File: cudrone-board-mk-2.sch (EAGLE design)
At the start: 61 parts, among them Q1 BSS138, U1 EDISON_CONNECTOR_FULLMOUNTING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, U2 FTS31XS-U, U4 TPS62065, U5 USD-SOCKETNEW, U6 TXB0108, U8 PCA9306, U9 MIC5205

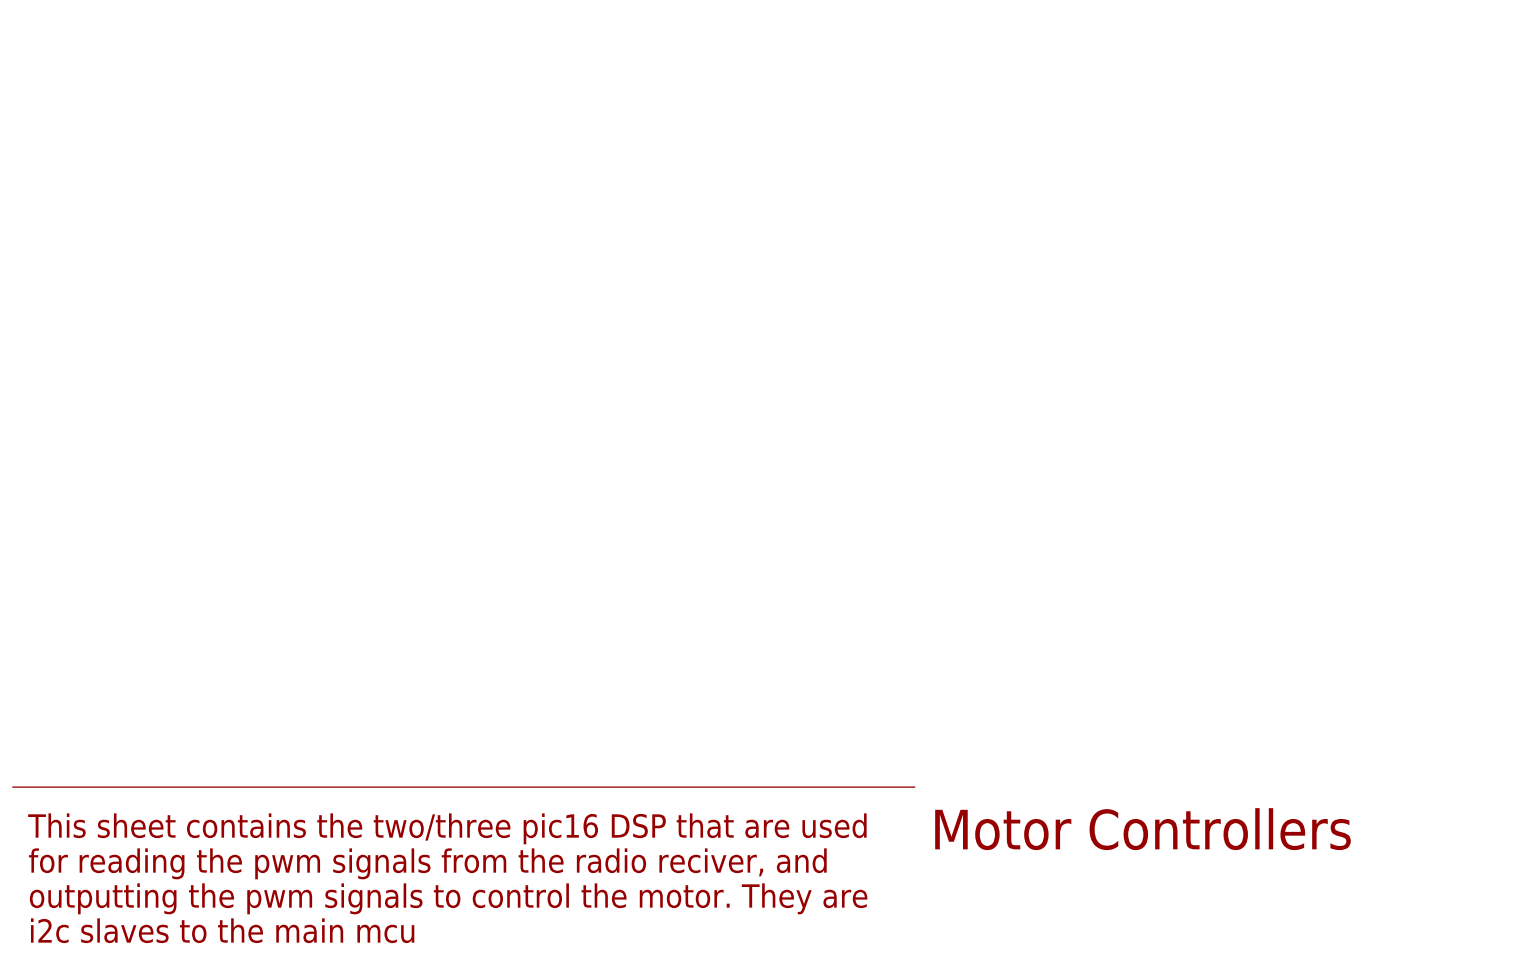
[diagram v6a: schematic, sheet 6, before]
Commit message: Added new port for servos on the motors to be connected. Picked a dsp to be used to control the motors
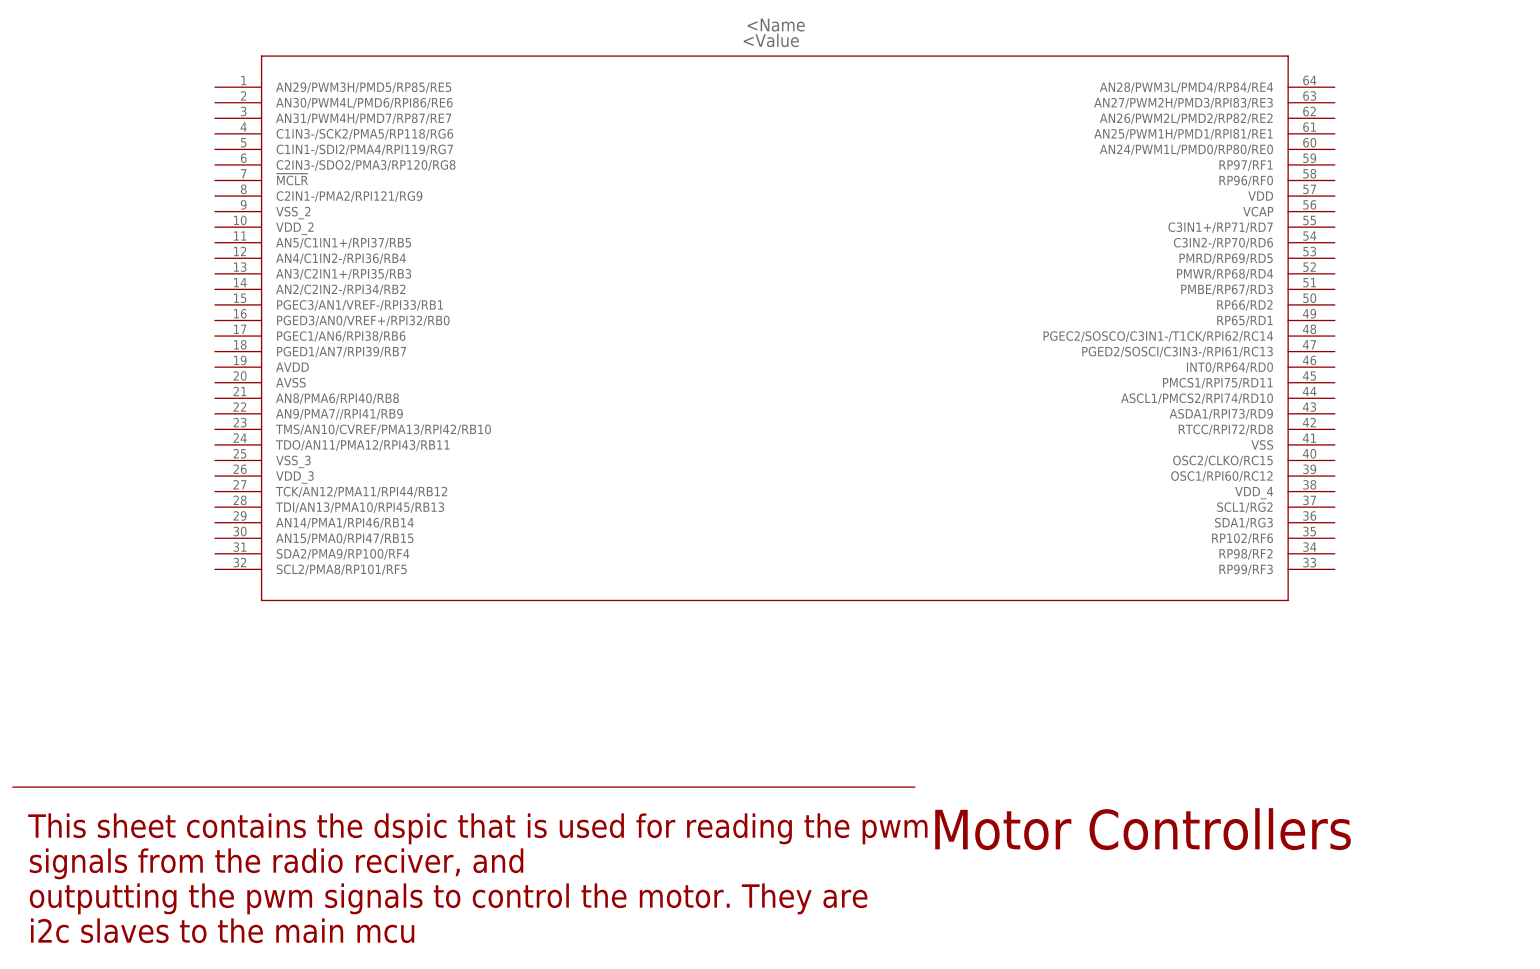
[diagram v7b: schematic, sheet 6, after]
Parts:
- added MOTOR_SERVO: 3X8, Drone_Connectors:3X8
- added U$4: DSPIC33EP512MC806-I/PT, DSPIC33EP512MC806:DSPIC33EP512MC806-I/PT
- renumbered SERVOS to GIMBAL_SERVOS
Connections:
- new net MS1: MOTOR_SERVO.8
- new net MS2: MOTOR_SERVO.7
- new net MS3: MOTOR_SERVO.6
- new net MS4: MOTOR_SERVO.5
- new net MS5: MOTOR_SERVO.4
- new net MS6: MOTOR_SERVO.3
- new net MS7: MOTOR_SERVO.2
- new net MS8: MOTOR_SERVO.1
- net 5V: now also MOTOR_SERVO.V
- net GND: now also MOTOR_SERVO.G
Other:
- note added: "This sheet contains the dspic that is used for reading the pwm signals from the radio reciver, and outputting the pwm signals to control the motor. They are i2c slaves to the main mcu"
- note removed: "This sheet contains the two/three pic16 DSP that are used for reading the pwm signals from the radio reciver, and outputting the pwm signals to control the motor. They are i2c slaves to the main mcu"
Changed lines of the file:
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@@
 <?xml version="1.0" encoding="utf-8"?>
 <!DOCTYPE eagle SYSTEM "eagle.dtd">
-<eagle version="6.5.0">
+<eagle version="8.0.0">
 <drawing>
 <settings>
@@
 <part name="SUPPLY22" library="SparkFun-Aesthetics" deviceset="1.8V" device=""/>
 <part name="SUPPLY23" library="SparkFun-Aesthetics" deviceset="1.8V" device=""/>
-<part name="SERVOS" library="Drone_Connectors" deviceset="3X4" device=""/>
+<part name="GIMBAL_SERVOS" library="Drone_Connectors" deviceset="3X4" device=""/>
 <part name="RECIVER" library="Drone_Connectors" deviceset="3X8" device=""/>
 <part name="ESC" library="Drone_Connectors" deviceset="3X8" device=""/>
@@
 <part name="GND35" library="SparkFun-Aesthetics" deviceset="GND" device=""/>
 <part name="GND36" library="SparkFun-Aesthetics" deviceset="GND" device=""/>
+<part name="MOTOR_SERVO" library="Drone_Connectors" deviceset="3X8" device=""/>
+<part name="SUPPLY27" library="SparkFun-Aesthetics" deviceset="5V" device=""/>
+<part name="GND37" library="SparkFun-Aesthetics" deviceset="GND" device=""/>
+<part name="U$4" library="DSPIC33EP512MC806" deviceset="DSPIC33EP512MC806-I/PT" device=""/>
 </parts>
 <sheets>
@@
 <text x="149.86" y="25.4" size="6.4516" layer="94">Motor Controllers</text>
 <wire x1="147.32" y1="35.56" x2="0" y2="35.56" width="0.1524" layer="94"/>
-<text x="2.54" y="10.16" size="3.81" layer="94">This sheet contains the two/three pic16 DSP that are used
-for reading the pwm signals from the radio reciver, and
+<text x="2.54" y="10.16" size="3.81" layer="94">This sheet contains the dspic that is used for reading the pwm
+signals from the radio reciver, and
 outputting the pwm signals to control the motor. They are
 i2c slaves to the main mcu</text>
@@
 <instance part="FRAME6" gate="G$1" x="0" y="0"/>
 <instance part="FRAME6" gate="G$2" x="147.32" y="0"/>
+<instance part="U$4" gate="A" x="33.02" y="149.86"/>
 </instances>
 <busses>
@@
 <instance part="FRAME9" gate="G$1" x="0" y="0"/>
 <instance part="FRAME9" gate="G$2" x="147.32" y="0"/>
-<instance part="SERVOS" gate="G$1" x="114.3" y="160.02"/>
+<instance part="GIMBAL_SERVOS" gate="G$1" x="114.3" y="160.02"/>
 <instance part="RECIVER" gate="G$1" x="114.3" y="129.54"/>
 <instance part="ESC" gate="G$1" x="114.3" y="91.44"/>
@@
 <instance part="GND35" gate="1" x="106.68" y="114.3"/>
 <instance part="GND36" gate="1" x="106.68" y="149.86"/>
+<instance part="MOTOR_SERVO" gate="G$1" x="114.3" y="55.88"/>
+<instance part="SUPPLY27" gate="G$1" x="106.68" y="66.04"/>
+<instance part="GND37" gate="1" x="106.68" y="40.64"/>
 </instances>
 <busses>
@@
 <pinref part="GND36" gate="1" pin="GND"/>
 <wire x1="106.68" y1="152.4" x2="106.68" y2="154.94" width="0.1524" layer="91"/>
-<pinref part="SERVOS" gate="G$1" pin="G"/>
+<pinref part="GIMBAL_SERVOS" gate="G$1" pin="G"/>
 <wire x1="106.68" y1="154.94" x2="109.22" y2="154.94" width="0.1524" layer="91"/>
 </segment>
@@
 <wire x1="106.68" y1="81.28" x2="109.22" y2="81.28" width="0.1524" layer="91"/>
 </segment>
+<segment>
+<pinref part="MOTOR_SERVO" gate="G$1" pin="G"/>
+<pinref part="GND37" gate="1" pin="GND"/>
+<wire x1="109.22" y1="45.72" x2="106.68" y2="45.72" width="0.1524" layer="91"/>
+<wire x1="106.68" y1="45.72" x2="106.68" y2="43.18" width="0.1524" layer="91"/>
+</segment>
 </net>
 <net name="5V" class="0">
@@
 <pinref part="SUPPLY24" gate="G$1" pin="5V"/>
 <wire x1="106.68" y1="165.1" x2="106.68" y2="162.56" width="0.1524" layer="91"/>
-<pinref part="SERVOS" gate="G$1" pin="V"/>
+<pinref part="GIMBAL_SERVOS" gate="G$1" pin="V"/>
 <wire x1="106.68" y1="162.56" x2="109.22" y2="162.56" width="0.1524" layer="91"/>
 </segment>
@@
 <wire x1="106.68" y1="99.06" x2="109.22" y2="99.06" width="0.1524" layer="91"/>
 </segment>
+<segment>
+<pinref part="MOTOR_SERVO" gate="G$1" pin="V"/>
+<pinref part="SUPPLY27" gate="G$1" pin="5V"/>
+<wire x1="109.22" y1="63.5" x2="106.68" y2="63.5" width="0.1524" layer="91"/>
+<wire x1="106.68" y1="63.5" x2="106.68" y2="66.04" width="0.1524" layer="91"/>
+</segment>
 </net>
 <net name="GP12_PWM0" class="0">
 <segment>
-<pinref part="SERVOS" gate="G$1" pin="S4"/>
+<pinref part="GIMBAL_SERVOS" gate="G$1" pin="S4"/>
 <wire x1="121.92" y1="162.56" x2="124.46" y2="162.56" width="0.1524" layer="91"/>
 <label x="124.46" y="162.56" size="1.778" layer="95" xref="yes"/>
@@
 <net name="GP13_PWM1" class="0">
 <segment>
-<pinref part="SERVOS" gate="G$1" pin="S3"/>
+<pinref part="GIMBAL_SERVOS" gate="G$1" pin="S3"/>
 <wire x1="121.92" y1="160.02" x2="147.32" y2="160.02" width="0.1524" layer="91"/>
 <label x="147.32" y="160.02" size="1.778" layer="95" xref="yes"/>
@@
 <net name="GP182_PWM2" class="0">
 <segment>
-<pinref part="SERVOS" gate="G$1" pin="S2"/>
+<pinref part="GIMBAL_SERVOS" gate="G$1" pin="S2"/>
 <wire x1="121.92" y1="157.48" x2="124.46" y2="157.48" width="0.1524" layer="91"/>
 <label x="124.46" y="157.48" size="1.778" layer="95" xref="yes"/>
@@
 <net name="GP183_PWM3" class="0">
 <segment>
-<pinref part="SERVOS" gate="G$1" pin="S1"/>
+<pinref part="GIMBAL_SERVOS" gate="G$1" pin="S1"/>
 <wire x1="121.92" y1="154.94" x2="147.32" y2="154.94" width="0.1524" layer="91"/>
 <label x="147.32" y="154.94" size="1.778" layer="95" xref="yes"/>
@@
 </segment>
 </net>
+<net name="MS1" class="0">
+<segment>
+<pinref part="MOTOR_SERVO" gate="G$1" pin="8"/>
+<wire x1="121.92" y1="63.5" x2="124.46" y2="63.5" width="0.1524" layer="91"/>
+<label x="121.92" y="63.5" size="1.778" layer="95"/>
+</segment>
+</net>
+<net name="MS2" class="0">
+<segment>
+<pinref part="MOTOR_SERVO" gate="G$1" pin="7"/>
+<wire x1="121.92" y1="60.96" x2="124.46" y2="60.96" width="0.1524" layer="91"/>
+<label x="121.92" y="60.96" size="1.778" layer="95"/>
+</segment>
+</net>
+<net name="MS3" class="0">
+<segment>
+<pinref part="MOTOR_SERVO" gate="G$1" pin="6"/>
+<wire x1="121.92" y1="58.42" x2="124.46" y2="58.42" width="0.1524" layer="91"/>
+<label x="121.92" y="58.42" size="1.778" layer="95"/>
+</segment>
+</net>
+<net name="MS4" class="0">
+<segment>
+<pinref part="MOTOR_SERVO" gate="G$1" pin="5"/>
+<wire x1="121.92" y1="55.88" x2="124.46" y2="55.88" width="0.1524" layer="91"/>
+<label x="121.92" y="55.88" size="1.778" layer="95"/>
+</segment>
+</net>
+<net name="MS5" class="0">
+<segment>
+<pinref part="MOTOR_SERVO" gate="G$1" pin="4"/>
+<wire x1="121.92" y1="53.34" x2="124.46" y2="53.34" width="0.1524" layer="91"/>
+<label x="121.92" y="53.34" size="1.778" layer="95"/>
+</segment>
+</net>
+<net name="MS6" class="0">
+<segment>
+<pinref part="MOTOR_SERVO" gate="G$1" pin="3"/>
+<wire x1="121.92" y1="50.8" x2="124.46" y2="50.8" width="0.1524" layer="91"/>
+<label x="121.92" y="50.8" size="1.778" layer="95"/>
+</segment>
+</net>
+<net name="MS7" class="0">
+<segment>
+<pinref part="MOTOR_SERVO" gate="G$1" pin="2"/>
+<wire x1="121.92" y1="48.26" x2="124.46" y2="48.26" width="0.1524" layer="91"/>
+<label x="121.92" y="48.26" size="1.778" layer="95"/>
+</segment>
+</net>
+<net name="MS8" class="0">
+<segment>
+<pinref part="MOTOR_SERVO" gate="G$1" pin="1"/>
+<wire x1="121.92" y1="45.72" x2="124.46" y2="45.72" width="0.1524" layer="91"/>
+<label x="121.92" y="45.72" size="1.778" layer="95"/>
+</segment>
+</net>

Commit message: Made their be a few less motor connectors so that everything fits on the dsp. Also added some reguator libraries
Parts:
- removed RECIVER: 3X8, Drone_Connectors:3X8
- removed S1: POWER, SparkFun-Electromechanical:SWITCH-MOMENTARY-2TACTILE-SWITCH-SMD-RIGHT-ANGLE
- added GIMBAL_SERVOS1: 3X4, Drone_Connectors:3X4
- added POWER: CANSAT_SWITCH, SparkFun-Electromechanical:CANSAT_SWITCH
- D2: value YELLOW -> Yellow
- ESC, MOTOR_SERVO: value 3X8 -> 3X6; device Drone_Connectors:3X8 -> Drone_Connectors:3X6
- Q1: value BSS138 -> 200mA/50V
- SJ4: device SparkFun-Passives:JUMPER-PAD-3-2OF3_NC_BY_TRACE -> SparkFun-Passives:JUMPER-PAD-3-2OF3_NC_BY_TRACE_LARGE
- renumbered U$4 to MOTOR_CONTROLLER
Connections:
- removed net AUX_0: RECIVER.4
- removed net AUX_1: RECIVER.3
- removed net AUX_2: RECIVER.2
- removed net AUX_3: RECIVER.1
- removed net M7: ESC.2
- removed net M8: ESC.1
- removed net MS7: MOTOR_SERVO.2
- removed net MS8: MOTOR_SERVO.1
- net 5V: now also GIMBAL_SERVOS1.V; no longer RECIVER.V
- net GND: now also GIMBAL_SERVOS1.G, POWER.O, U9.EN; no longer RECIVER.G, S1.2, U9.GND
- net GP77_SD_0_CD#: now also U5.CD1; no longer U5.SHIELD@2
- net N$15: now also POWER.P; no longer S1.1
- net PITCH: now also GIMBAL_SERVOS1.S4; no longer RECIVER.8
- net ROLL: now also GIMBAL_SERVOS1.S3; no longer RECIVER.7
- net THROTTLE: now also GIMBAL_SERVOS1.S1; no longer RECIVER.5
- net VSYS: now also U9.GND; no longer U9.EN
- net YAW: now also GIMBAL_SERVOS1.S2; no longer RECIVER.6
